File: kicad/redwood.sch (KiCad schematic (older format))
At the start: 39 parts, among them J1 Haptic, J2 TRRS, K1 diode-choc, K10 diode-choc, K11 diode-choc, K12 diode-choc, K13 diode-choc, K14 diode-choc, K15 diode-choc, K16 diode-choc, K17 diode-choc, K18 diode-choc, K19 diode-choc, K2 diode-choc, K20 choc_rotary, K21 diode-choc, K22 diode-choc, K23 diode-choc, K24 diode-choc, K3 diode-choc, K4 diode-choc, K5 diode-choc, K6 diode-choc, K7 diode-choc, K8 diode-choc, K9 diode-choc, SW1 Reset, U1 ProMicro_r

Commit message: Cleanup symbol references
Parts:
- H1: symbol redwood:Tenting_Mounts -> redwood:Tenting_Mount
- H2: symbol redwood:Trackball_Mounts -> redwood:Trackball_Mount
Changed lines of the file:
@@
 	1950 6400 2250 6400
 $Comp
-L redwood:Trackball_Mounts H2
+L redwood:Trackball_Mount H2
 U 1 1 614FB6B6
 P 8700 5450
@@
 $EndComp
 $Comp
-L redwood:Tenting_Mounts H1
+L redwood:Tenting_Mount H1
 U 1 1 6147F195
 P 8700 4950

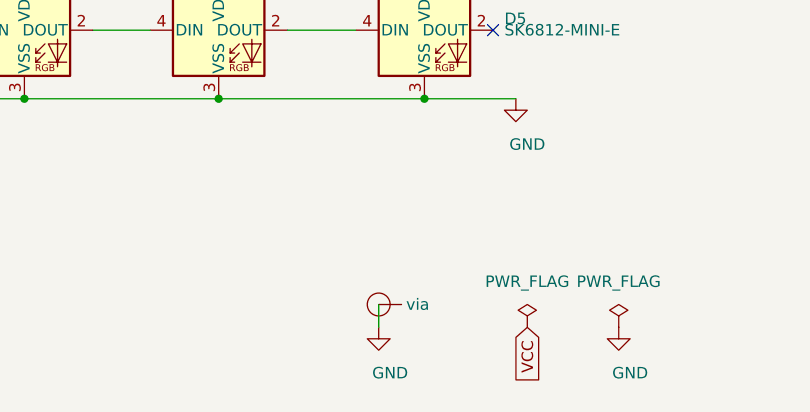
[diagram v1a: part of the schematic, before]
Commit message: scheme: extra stitching via
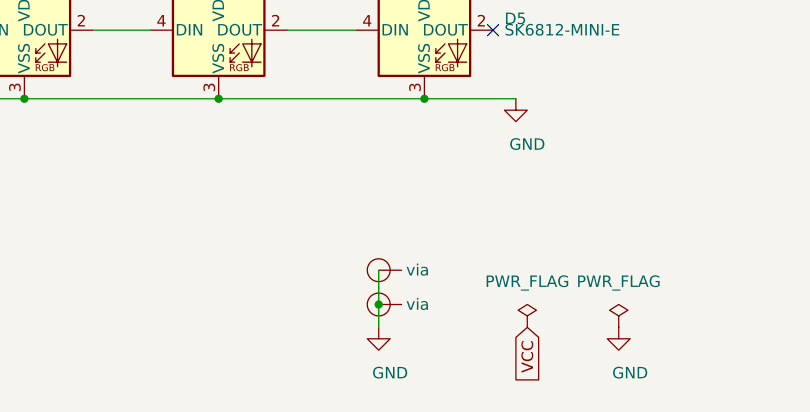
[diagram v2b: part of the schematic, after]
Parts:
- added V2: Via, mmccoyd:VIA-0.8mm, symbol redwood:Via
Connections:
- net GND: now also V2.1 (via)
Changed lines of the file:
@@
 Wire Wire Line
 	4950 7700 4950 7600
+$Comp
+L redwood:Via V2
+U 1 1 615E1C4E
+P 4950 7450
+F 0 "V2" H 5150 7450 50  0001 C BNN
+F 1 "Via" H 4950 7200 50  0001 C CNN
+F 2 "mmccoyd:VIA-0.8mm" H 4950 7350 50  0001 C CNN
+F 3 "" H 4950 7450 50  0001 C CNN
+	1    4950 7450
+	1    0    0    -1
+$EndComp
+Wire Wire Line
+	4950 7450 4950 7600
+Connection ~ 4950 7600
 $EndSCHEMATC

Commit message: Symbols and footprints all from project libs
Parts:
- D6: symbol ki_device:D_Small -> redwood:D_Small
- J1: symbol MMLid:Conn_01x05-Connector_Generic -> redwood:Conn_01x05-Connector_Generic
- R1, R2: symbol ki_device:R -> redwood:R
- SW1: symbol kbd:SW_PUSH -> redwood:SW_PUSH
- U1: symbol kbd:ProMicro_r -> redwood:ProMicro_r
- V1, V2: footprint mmccoyd:VIA-0.8mm -> redwood:VIA-0.8mm
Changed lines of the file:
@@
 $EndDescr
 $Comp
-L pwr:GND #PWR04
+L redwood:GND #PWR04
 U 1 1 6120BEE9
 P 7150 4750
@@
 reset
 $Comp
-L kbd:ProMicro_r U1
+L redwood:ProMicro_r U1
 U 1 1 6162C399
 P 6750 3900
@@
 row3
 $Comp
-L pwr:GND #PWR03
+L redwood:GND #PWR03
 U 1 1 61711229
 P 7875 3400
@@
 $EndComp
 $Comp
-L pwr:PWR_FLAG #FLG01
+L redwood:PWR_FLAG #FLG01
 U 1 1 618AC0F3
 P 5600 7700
@@
 	5700 3300 6100 3300
 $Comp
-L pwr:GND #PWR02
+L redwood:GND #PWR02
 U 1 1 618DD7B5
 P 5700 3300
@@
 $EndComp
 $Comp
-L pwr:PWR_FLAG #FLG02
+L redwood:PWR_FLAG #FLG02
 U 1 1 618AB37B
 P 6000 7700
@@
 $EndComp
 $Comp
-L pwr:GND #PWR06
+L redwood:GND #PWR06
 U 1 1 614248F7
 P 6000 7700
@@
 VCC
 $Comp
-L pwr:GND #PWR05
+L redwood:GND #PWR05
 U 1 1 61436F2E
 P 5550 6700
@@
 NoConn ~ 6100 3200
 $Comp
-L MMLid:Conn_01x05-Connector_Generic J1
+L redwood:Conn_01x05-Connector_Generic J1
 U 1 1 616B8147
 P 8900 4300
@@
 SDA
 $Comp
-L pwr:GND #PWR07
+L redwood:GND #PWR07
 U 1 1 616C872C
 P 8375 4100
@@
 	2250 4700 1950 4550
 $Comp
-L ki_device:R R2
+L redwood:R R2
 U 1 1 618CD67C
 P 6900 5500
@@
 SDA
 $Comp
-L ki_device:R R1
+L redwood:R R1
 U 1 1 618CC9AE
 P 6900 5250
@@
 VCC
 $Comp
-L pwr:GND #PWR09
+L redwood:GND #PWR09
 U 1 1 61A733F7
 P 8350 3700
@@
 Connection ~ 8350 3700
 $Comp
-L kbd:SW_PUSH SW1
+L redwood:SW_PUSH SW1
 U 1 1 6120A557
 P 6850 4750
@@
 	1950 4650 2050 4700
 $Comp
-L ki_device:D_Small D6
+L redwood:D_Small D6
 U 1 1 61519A6F
 P 2050 4550
@@
 Connection ~ 2550 4550
 $Comp
-L pwr:GND #PWR0101
+L redwood:GND #PWR0101
 U 1 1 61525DEF
 P 1500 5100
@@
 F 0 "V1" H 5150 7600 50  0001 C BNN
 F 1 "Via" H 4950 7350 50  0001 C CNN
-F 2 "mmccoyd:VIA-0.8mm" H 4950 7500 50  0001 C CNN
+F 2 "redwood:VIA-0.8mm" H 4950 7500 50  0001 C CNN
 F 3 "" H 4950 7600 50  0001 C CNN
 	1    4950 7600
@@
 $EndComp
 $Comp
-L pwr:GND #PWR0102
+L redwood:GND #PWR0102
 U 1 1 615FED02
 P 4950 7700
@@
 F 0 "V2" H 5150 7450 50  0001 C BNN
 F 1 "Via" H 4950 7200 50  0001 C CNN
-F 2 "mmccoyd:VIA-0.8mm" H 4950 7350 50  0001 C CNN
+F 2 "redwood:VIA-0.8mm" H 4950 7350 50  0001 C CNN
 F 3 "" H 4950 7450 50  0001 C CNN
 	1    4950 7450

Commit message: Common cathode diodes for key matrix
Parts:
- removed D6: Diode, redwood:D_SOD-123_rev, symbol redwood:D_Small
- removed K1, K10, K11, K12, K13, K14, K15, K16, K17, K18, K19, K2, K21, K22, K23, K24, K3, K4, K5, K6, K7, K8, K9: diode-choc, redwood:pg1350-DR, symbol redwood:diode-choc
- added D10, D11, D12, D13, D14, D15, D16, D17, D18, D7, D8, D9: BAV70, ki_syms:SOT-23, symbol ki_syms:BAV70
- added K1, K10, K11, K12, K13, K14, K15, K16, K17, K18, K19, K2, K21, K22, K23, K24, K3, K4, K5, K6, K7, K8, K9: SW_Key, redwood:pg1350-R, symbol redwood:SW_Key
- D1, D2, D3, D4, D5: footprint redwood:SK6812-MINI-E -> ki_syms:SK6812-MINI-E; symbol redwood:SK6812-MINI-E -> ki_syms:SK6812-MINI-E
- J1: symbol redwood:Conn_01x05-Connector_Generic -> ki_syms:Conn_01x05-Connector_Generic
- K20: value choc_rotary -> SW_Rotary; symbol redwood:choc_rotary -> redwood:SW_Rotary
- R1, R2: footprint redwood:R_0805_2012Metric -> ki_syms:R_0805_2012Metric; symbol redwood:R -> ki_syms:R
- SW1: footprint redwood:SW_Tactile_SPST_Angled_MJTP1117 -> ki_syms:SW_Tactile_SPST_Angled_MJTP1117
- V1, V2: footprint redwood:VIA-0.8mm -> ki_syms:VIA-0.8mm; symbol redwood:Via -> ki_syms:Via
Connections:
- net col0: now also K1.1, K13.1, K7.1
- net col1: now also K14.1, K2.1, K21.1, K8.1
- net col2: now also K15.1, K22.1, K3.1, K9.1
- net col3: now also K10.1, K16.1, K23.1, K4.1
- net col4: now also K11.1, K17.1, K24.1, K5.1
- net col5: now also K12.1, K18.1, K19.1, K6.1
- net row0: now also D7.3 (K), D8.3 (K), D9.3 (K)
- net row1: now also D10.3 (K), D11.3 (K), D12.3 (K)
- net row2: now also D13.3 (K), D14.3 (K), D15.3 (K)
- net row3: now also D16.3 (K), D17.3 (K), D18.3 (K)
- net at K20.S2: now also D16.1 (A)
- new net: D13.1 (A), K13.2
- new net: D13.2 (A), K14.2
- new net: D7.1 (A), K1.2
- new net: D7.2 (A), K2.2
- new net: D18.1 (A), K19.2
- new net: D18.2 (A), K24.2
- new net: D11.1 (A), K9.2
- new net: D11.2 (A), K10.2
- new net: D14.1 (A), K15.2
- new net: D14.2 (A), K16.2
- new net: D9.1 (A), K5.2
- new net: D9.2 (A), K6.2
- new net: D12.1 (A), K11.2
- new net: D12.2 (A), K12.2
- new net: D15.1 (A), K17.2
- new net: D15.2 (A), K18.2
- new net: D8.1 (A), K3.2
- new net: D8.2 (A), K4.2
- new net: D10.1 (A), K7.2
- new net: D10.2 (A), K8.2
- new net: D16.2 (A), K21.2
- new net: D17.1 (A), K22.2
- new net: D17.2 (A), K23.2
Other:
- moved on the sheet: H1, H2, J1, J2, K20, R1, R2, SW1, U1

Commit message: Battery support, Hillside logo, mounting holes
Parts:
- added C1: 4u7, ki_syms:C_0805_2012Metric, symbol ki_syms:C
- added H3: Scene, redwood:Hillside_Scene, symbol redwood:Scene
- added H4, H5, H8, H9: MountHole, ki_mount_hole:MountingHole_2.2mm_M2_Pad, symbol ki_mech:MountingHole
- added H6, H7: MountHole, ki_mount_hole:MountingHole_2.2mm_M2, symbol ki_mech:MountingHole
- added J3: Batt_Pos, ki_syms:1pin_conn, symbol ki_conn_generic:Conn_01x01
- added J4: Batt_GND, ki_syms:1pin_conn, symbol ki_conn_generic:Conn_01x01
- added JP1: SolderJumper_2_Bridged, ki_syms:SolderJumper-2_P1.3mm_Bridged_RoundedPad1.0x1.5mm, symbol ki_jumper:SolderJumper_2_Bridged
- added SW2: SW_Power, ki_syms:SW_SPDT_JS202011AQN, symbol ki_switch:SW_SPDT
- added V10, V11, V12, V13, V14, V15, V16, V17, V18, V19, V3, V4, V5, V6, V7, V8, V9: Via, ki_syms:VIA-0.8mm, symbol ki_syms:Via
- H1: value Tenting_Mount -> Mount_Tenting; symbol redwood:Tenting_Mount -> redwood:Mount_Tenting
- H2: symbol redwood:Trackball_Mount -> redwood:Mount_Trackball
- SW1: footprint ki_syms:SW_Tactile_SPST_Angled_MJTP1117 -> ki_syms:SW_SPST_SKQG_WithStem
- V1: value Via -> V
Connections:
- net GND: now also C1.2, J4.1 (Pin_1), V10.1 (via), V11.1 (via), V12.1 (via), V13.1 (via), V14.1 (via), V15.1 (via), V16.1 (via), V17.1 (via), V18.1 (via), V19.1 (via), V3.1 (via), V4.1 (via), V5.1 (via), V6.1 (via), V7.1 (via), V8.1 (via), V9.1 (via)
- net VCC: now also JP1.1 (A); no longer D1.1 (VDD), D2.1 (VDD), D3.1 (VDD), D4.1 (VDD), D5.1 (VDD), J1.5 (Pin_5), R1.1, R2.1
- net raw: now reaches U1.24 (RAW)
- net raw: now also C1.1, SW2.3 (C)
- new net VCC_ACC: D1.1 (VDD), D2.1 (VDD), D3.1 (VDD), D4.1 (VDD), D5.1 (VDD), J1.5 (Pin_5), JP1.2 (B), R1.1, R2.1
- new net bat+: J3.1 (Pin_1), SW2.2 (B)
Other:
- note added: "Accessories"
- note added: "Power for Nice!nano"
- note added: "Stiching vias"
- moved on the sheet: D1, D2, D3, D4, D5, H1, H2, J1, J2, R1, R2, SW1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
